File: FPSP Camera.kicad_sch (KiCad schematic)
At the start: 81 parts, among them J1 Conn_01x24_Socket, J2 Conn_01x02, J3 Conn_02x07_Counter_Clockwise, J4 Conn_02x07_Counter_Clockwise, J5 SM03B-SRSS-TB, J6 USB_B_Micro, J7 Conn_02x06_Odd_Even, U1 ICM-45686, U2 W25Q128JVS, U3 RP2350_60QFN, U4 TLV75533PDRV, U5 TLV73328PDRV, U6 TLV73315PDRV, Y1 SiT8008xx-1x-xxE

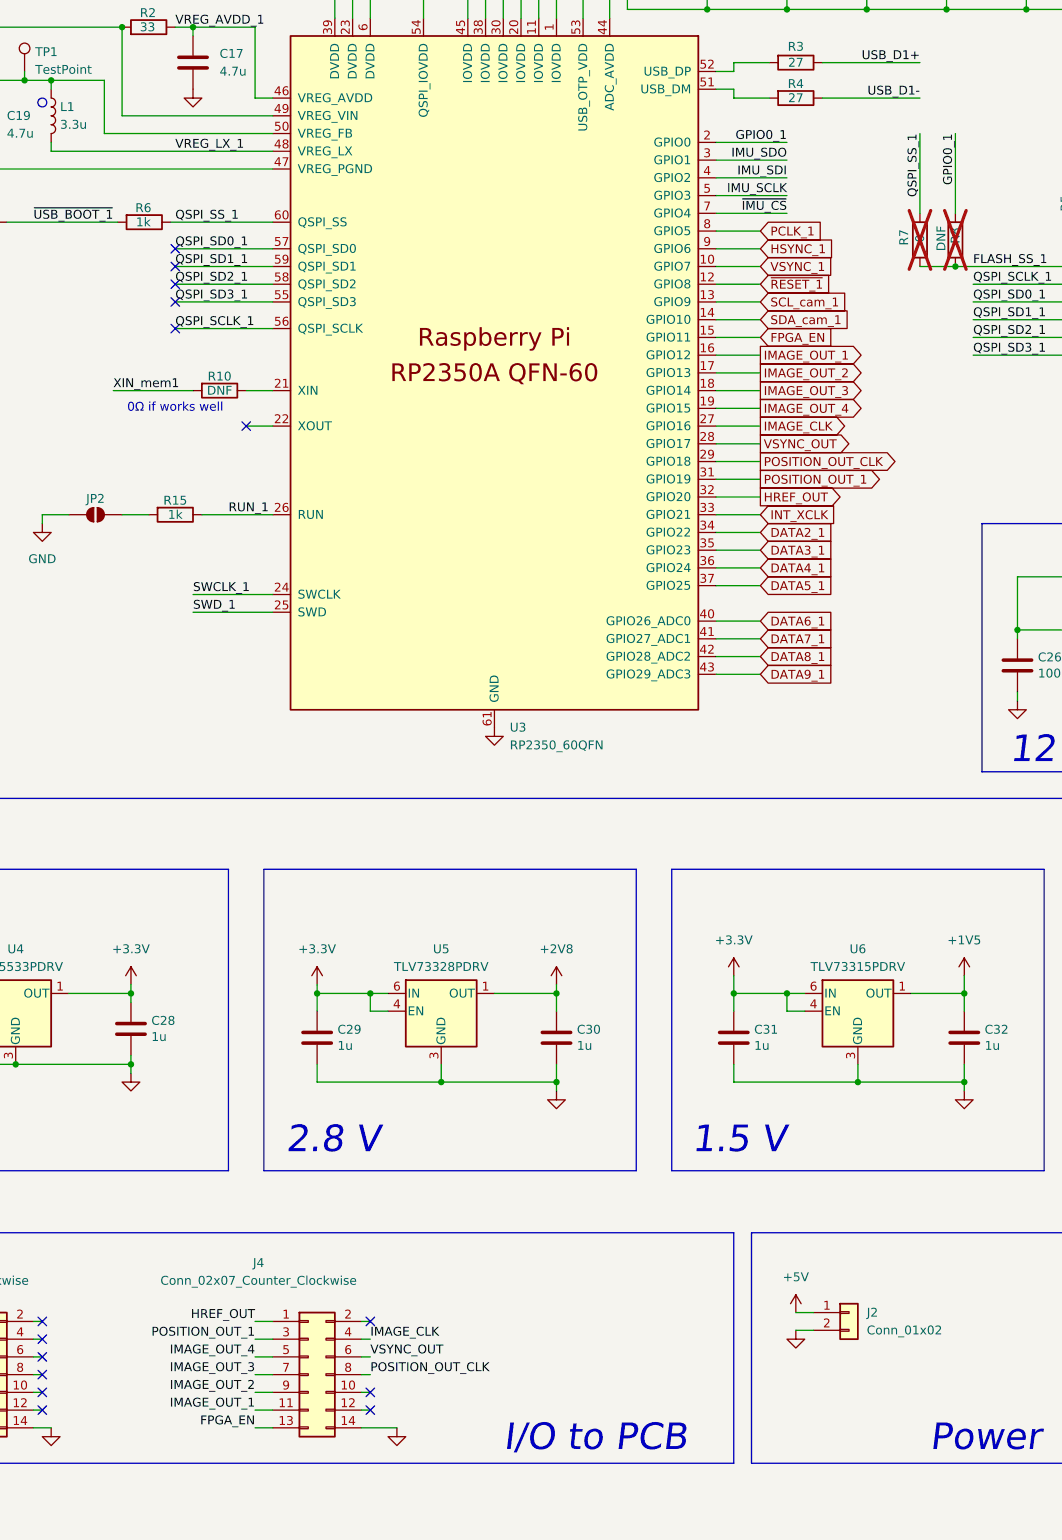
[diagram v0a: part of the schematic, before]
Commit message: GPIO_1 added
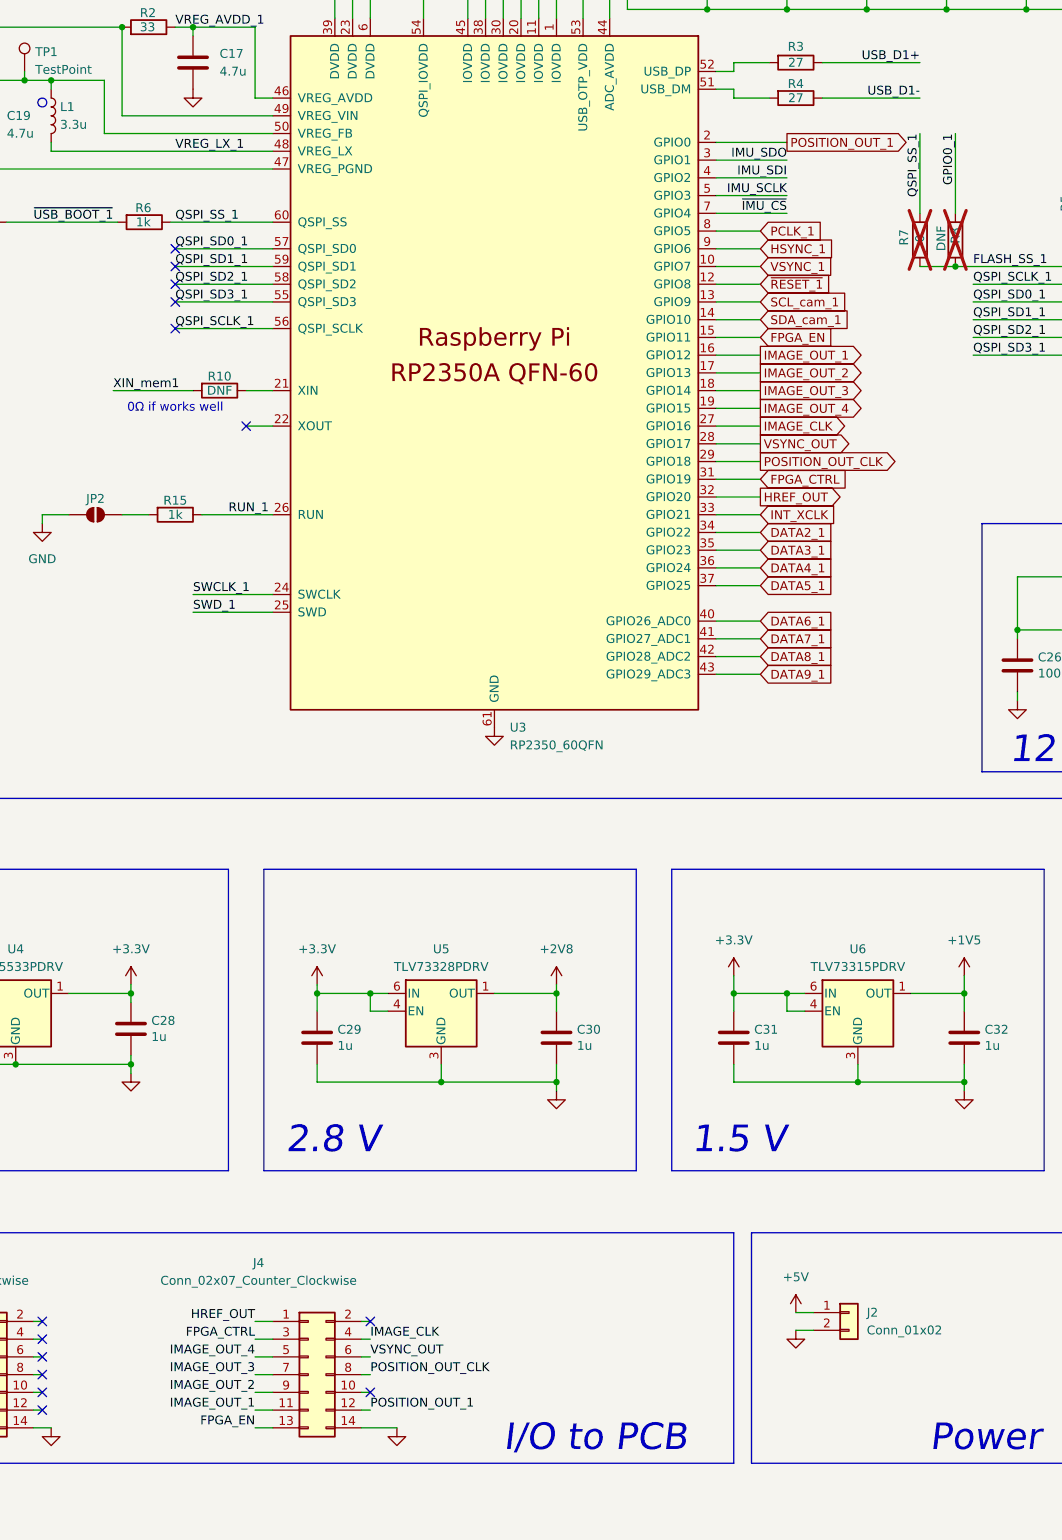
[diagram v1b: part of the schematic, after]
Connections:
- net GPIO0_1: no longer U3.2 (GPIO0)
- net POSITION_OUT_1: now also J4.12 (Pin_12), U3.2 (GPIO0); no longer J4.3 (Pin_3), U3.31 (GPIO19)
- new net FPGA_CTRL: J4.3 (Pin_3), U3.31 (GPIO19)
- no-connect marks 34 -> 33
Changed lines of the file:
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@@
 	)
 	(no_connect
-		(at 57.15 265.43)
+		(at 104.14 255.27)
 	)
 	(no_connect
-		(at 76.2 109.22)
+		(at 57.15 265.43)
 	)
 	(no_connect
-		(at 104.14 267.97)
+		(at 76.2 109.22)
 	)
 	(no_connect
@@
 	)
 	(no_connect
-		(at 104.14 255.27)
-	)
-	(no_connect
 		(at 112.395 321.31)
 	)
@@
 		)
 	)
-	(label "GPIO0_1"
-		(at 163.83 86.36 180)
-		(effects
-			(font
-				(size 1.27 1.27)
-			)
-			(justify right bottom)
-		)
-	)
 	(label "RUN_1"
 		(at 83.82 139.7 0)
@@
 		)
 	)
+	(label "POSITION_OUT_1"
+		(at 104.14 267.97 0)
+		(effects
+			(font
+				(size 1.27 1.27)
+			)
+			(justify left bottom)
+		)
+	)
 	(label "HREF_OUT"
 		(at 87.63 255.27 180)
@@
 		)
 	)
-	(label "POSITION_OUT_1"
-		(at 87.63 257.81 180)
-		(effects
-			(font
-				(size 1.27 1.27)
-			)
-			(justify right bottom)
-		)
-	)
 	(label "~{RESET_1}"
 		(at 323.85 139.7 0)
@@
 		)
 	)
+	(label "FPGA_CTRL"
+		(at 87.63 257.81 180)
+		(effects
+			(font
+				(size 1.27 1.27)
+			)
+			(justify right bottom)
+		)
+	)
 	(label "SDA_cam_1"
 		(at 323.85 129.54 0)
@@
 		)
 	)
+	(global_label "POSITION_OUT_1"
+		(shape output)
+		(at 163.83 86.36 0)
+		(fields_autoplaced yes)
+		(effects
+			(font
+				(size 1.27 1.27)
+			)
+			(justify left)
+		)
+		(property "Intersheetrefs" "${INTERSHEET_REFS}"
+			(at 182.2367 86.36 0)
+			(hide yes)
+			(show_name no)
+			(do_not_autoplace no)
+			(effects
+				(font
+					(size 1.27 1.27)
+				)
+				(justify left)
+			)
+		)
+	)
 	(global_label "DATA2_1"
 		(shape input)
@@
 		)
 	)
-	(global_label "POSITION_OUT_1"
-		(shape output)
-		(at 160.02 134.62 0)
-		(fields_autoplaced yes)
-		(effects
-			(font
-				(size 1.27 1.27)
-			)
-			(justify left)
-		)
-		(property "Intersheetrefs" "${INTERSHEET_REFS}"
-			(at 178.4267 134.62 0)
-			(hide yes)
-			(show_name no)
-			(do_not_autoplace no)
-			(effects
-				(font
-					(size 1.27 1.27)
-				)
-				(justify left)
-			)
-		)
-	)
 	(global_label "VSYNC_1"
 		(shape output)
@@
 			(hide yes)
 			(show_name no)
+			(do_not_autoplace no)
+			(effects
+				(font
+					(size 1.27 1.27)
+				)
+				(justify left)
+			)
+		)
+	)
+	(global_label "FPGA_CTRL"
+		(shape input)
+		(at 160.02 134.62 0)
+		(fields_autoplaced yes)
+		(effects
+			(font
+				(size 1.27 1.27)
+			)
+			(justify left)
+		)
+		(property "Intersheetrefs" "${INTERSHEET_REFS}"
+			(at 173.2257 134.62 0)
+			(hide yes)
+			(show_name no)

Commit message: layout refined
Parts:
- removed D4: LED, Diode_SMD:D_0603_1608Metric, symbol Device:LED
- removed R21: 10k, Resistor_SMD:R_0402_1005Metric, symbol Device:R
- added TP3: 1V5, TestPoint:TestPoint_Pad_D1.0mm, symbol Connector:TestPoint
- TP1: value TestPoint -> 1V1
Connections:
- net +1V5: now also TP3.1

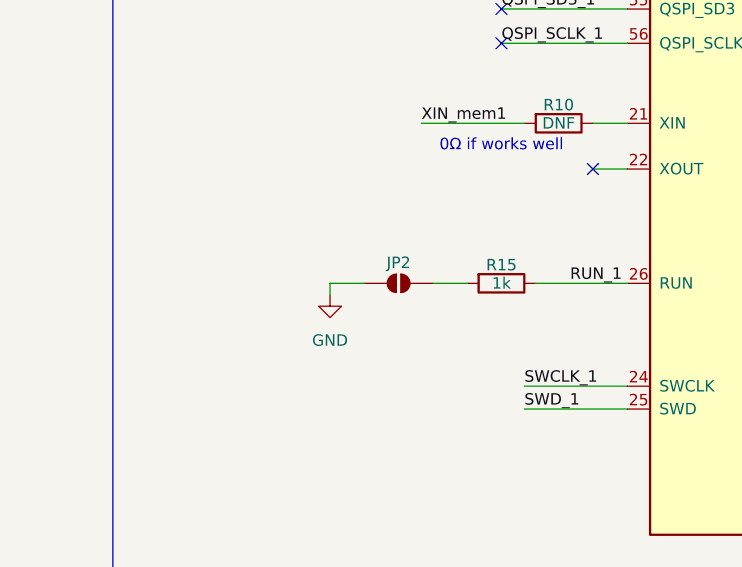
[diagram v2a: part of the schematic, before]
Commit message: Rpi Buck layout refined
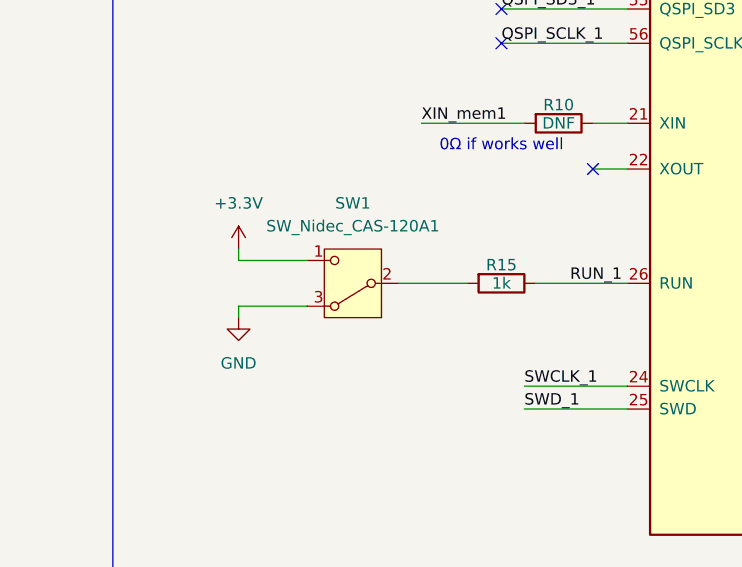
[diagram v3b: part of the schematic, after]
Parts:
- removed JP2: SolderJumper_2_Open, Jumper:SolderJumper-2_P1.3mm_Open_RoundedPad1.0x1.5mm, symbol Jumper:SolderJumper_2_Open
- added SW1: SW_Nidec_CAS-120A1, Button_Switch_SMD:Nidec_Copal_CAS-120A, symbol Switch:SW_Nidec_CAS-120A1
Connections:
- net +3.3V: now also SW1.1 (C)
- net GND: now also SW1.3 (A)
- net at R15.2: now also SW1.2 (B)

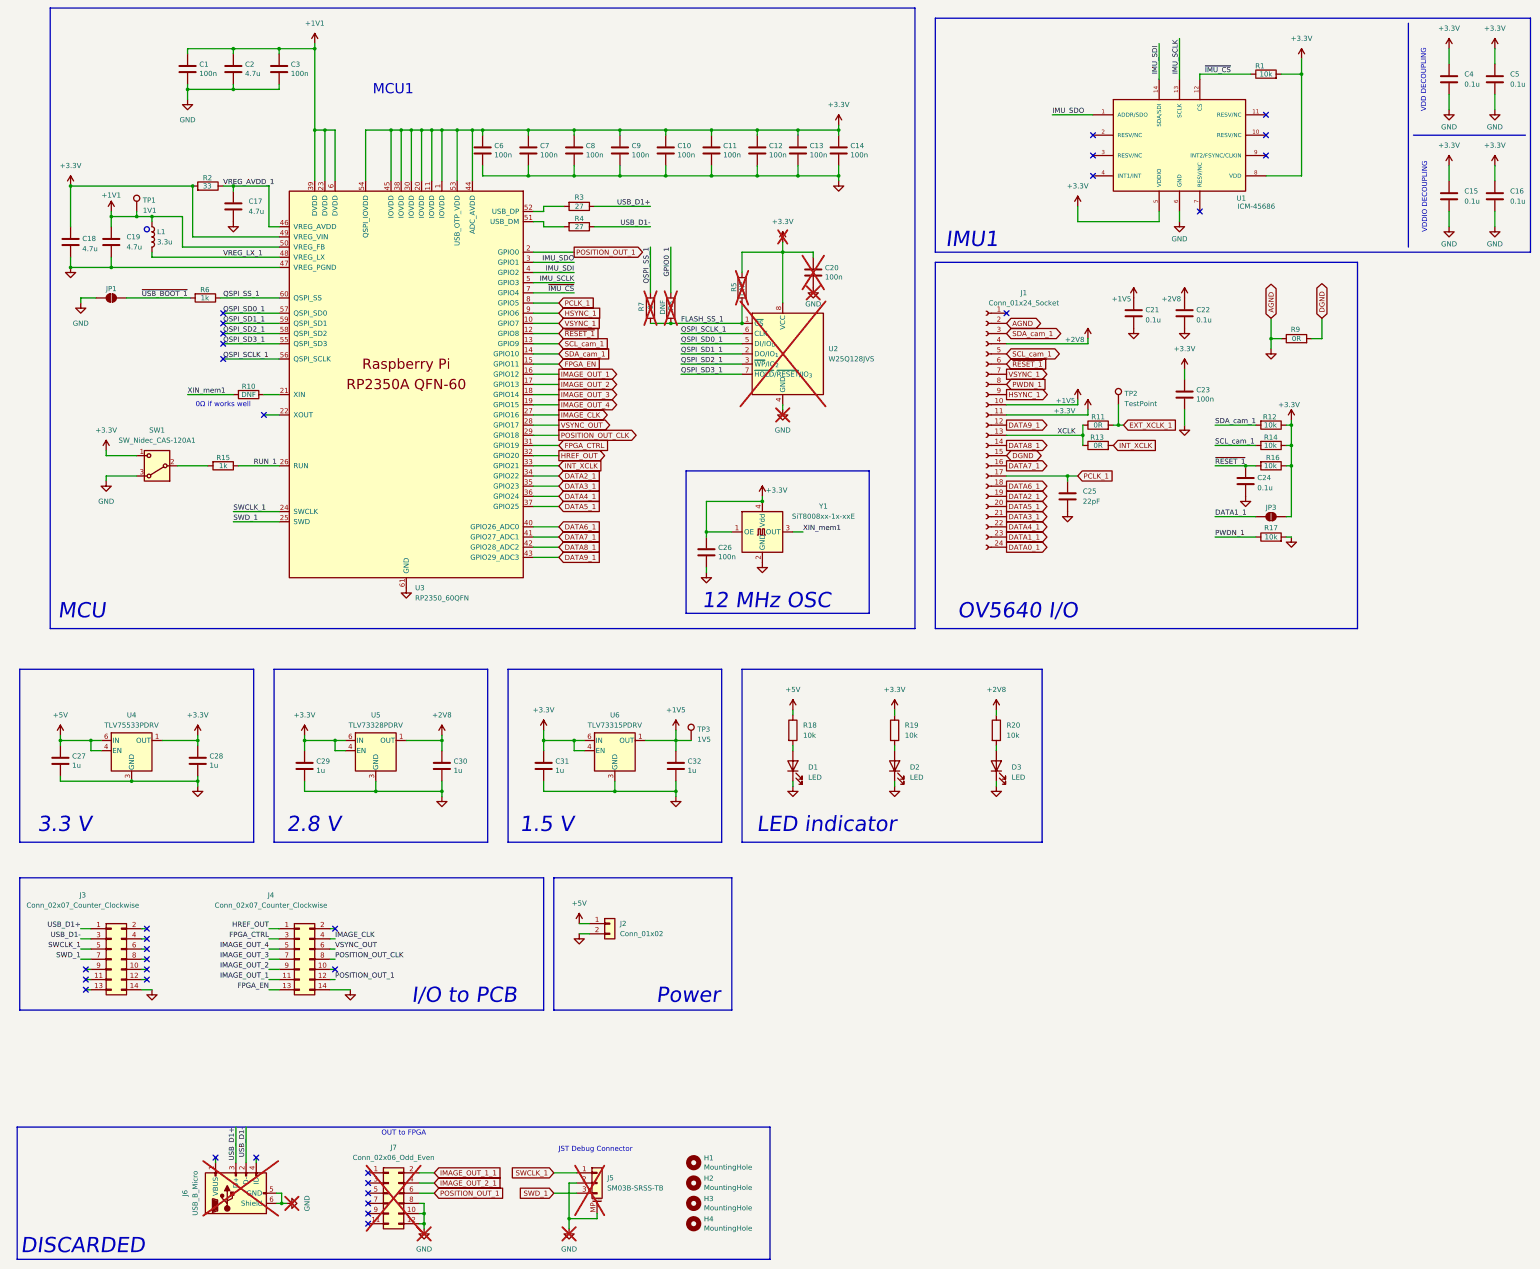
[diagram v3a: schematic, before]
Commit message: push button added; IMU updated
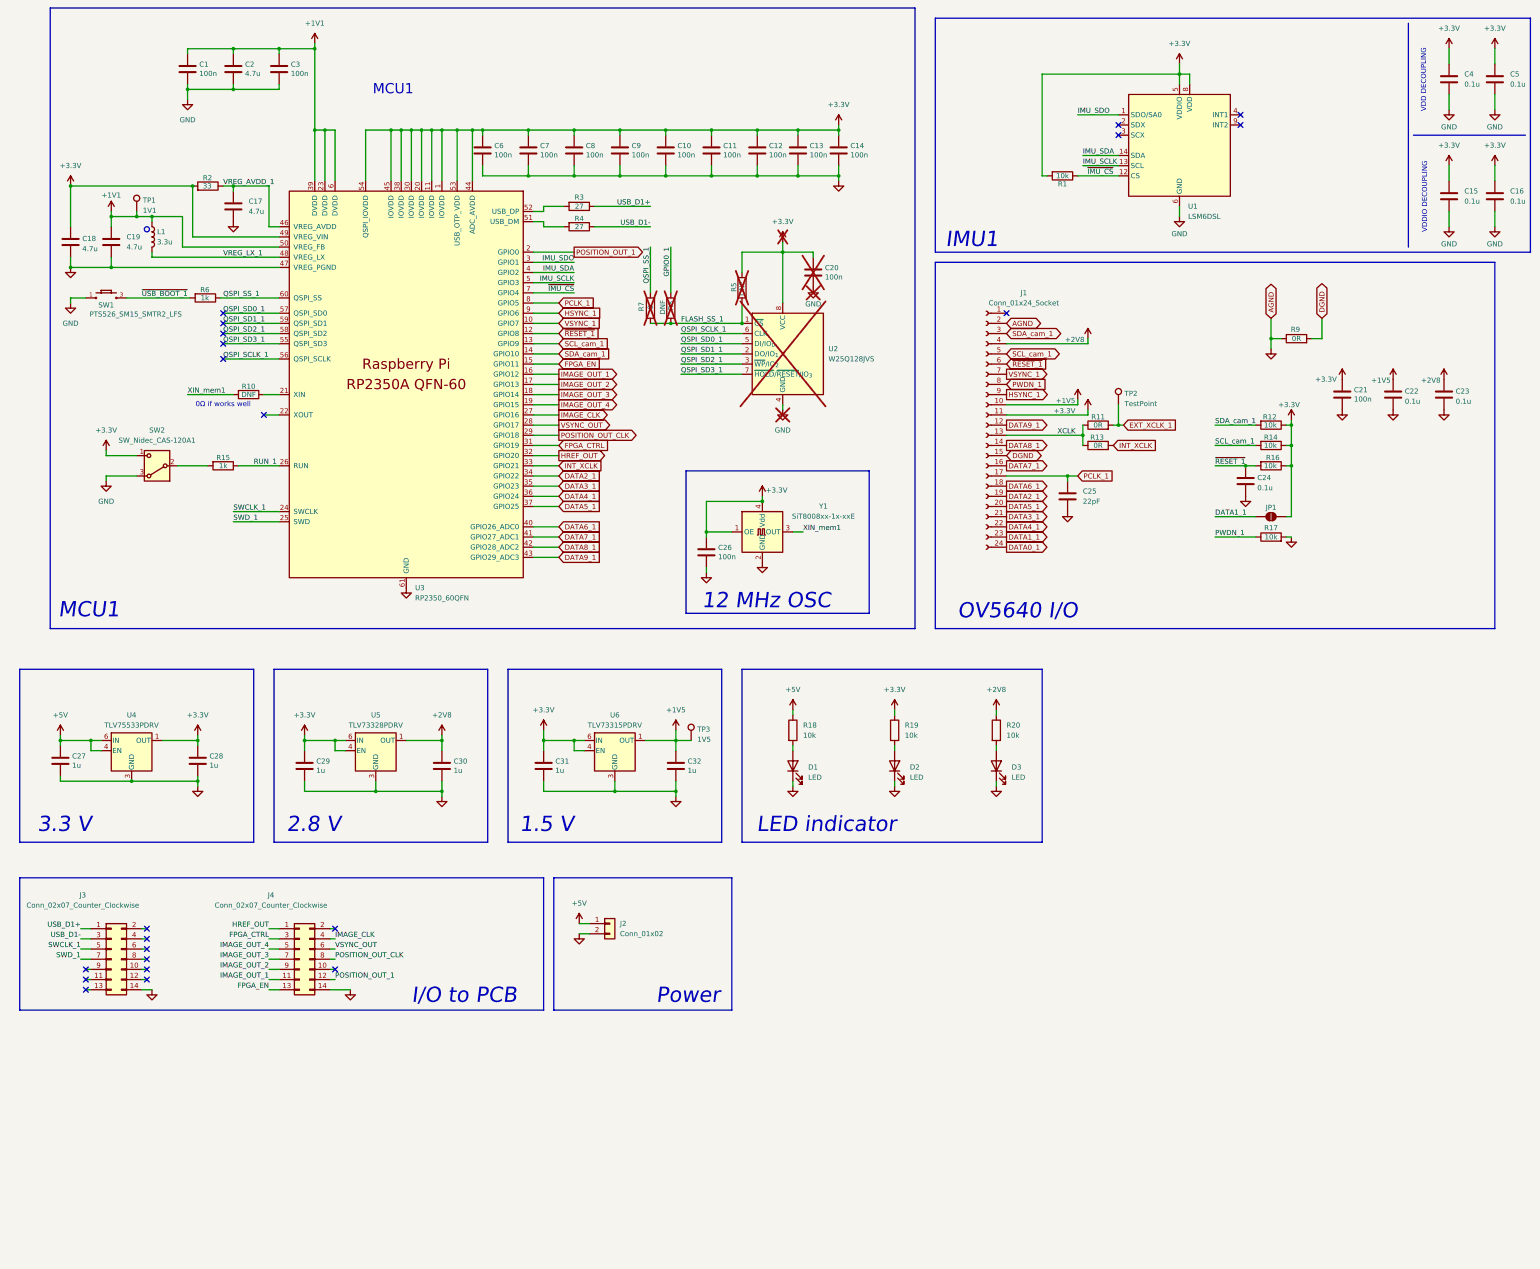
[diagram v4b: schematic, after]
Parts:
- removed H1, H2, H3, H4: MountingHole, MountingHole:MountingHole_2.7mm_M2.5, symbol Mechanical:MountingHole
- removed J5: SM03B-SRSS-TB, Connector_JST:JST_SH_SM03B-SRSS-TB_1x03-1MP_P1.00mm_Horizontal, symbol Connector_Generic_MountingPin:Conn_01x03_MountingPin
- removed J6: USB_B_Micro, RP2350_60QFN_minimal:USB_Micro-B_Amphenol_10103594-0001LF_Horizontal_modified, symbol Connector:USB_B_Micro
- removed J7: Conn_02x06_Odd_Even, Connector_PinHeader_2.54mm:PinHeader_2x06_P2.54mm_Vertical, symbol Connector_Generic:Conn_02x06_Odd_Even
- removed JP1: SolderJumper_2_Open, Jumper:SolderJumper-2_P1.3mm_Open_RoundedPad1.0x1.5mm, symbol Jumper:SolderJumper_2_Open
- removed U1: ICM-45686, ICM_45686:IC_ICM-45686, symbol ICM-45686:ICM-45686
- added SW1: PTS526_SM15_SMTR2_LFS, PTS526_SM15_SMTR2_LFS:PTS526SM15SMTR2LFS, symbol PTS526_SM15_SMTR2_LFS:PTS526_SM15_SMTR2_LFS
- added U1: LSM6DSL, Package_LGA:LGA-14_3x2.5mm_P0.5mm_LayoutBorder3x4y, symbol Sensor_Motion:LSM6DSL
- renumbered C23 to C21, C21 to C22, C22 to C23, JP3 to JP1, SW1 to SW2
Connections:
- net +3.3V: now also U1.5 (VDDIO), U1.8 (VDD)
- net GND: now also SW1.1, SW1.2, U1.6 (GND), U1.7 (GND)
- net IMU_SCLK: now also U1.13 (SCL)
- net IMU_SDO: now also U1.1 (SDO/SA0)
- net ~{IMU_CS}: now also U1.12 (CS)
- net ~{USB_BOOT_1}: now also SW1.3, SW1.4
- net IMU_SDI renamed IMU_SDA
- net IMU_SDA: now also U1.14 (SDA)
- no-connect marks 33 -> 22
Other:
- note removed: "DISCARDED"
- note removed: "JST Debug Connector"
- note removed: "MCU"
- note removed: "OUT to FPGA"
- moved on the sheet: C21, C22, C23
